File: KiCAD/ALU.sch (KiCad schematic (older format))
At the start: 55 parts, among them Q501 Q_NPN_CBE, Q502 Q_NPN_CBE, U501 74LS86AN, U502 74HCT32N, U503 74HCT32N, U504 74LS04, U505 74HCT157N, U506 74LS86AN, U507 74LS153, U508 74LS283N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

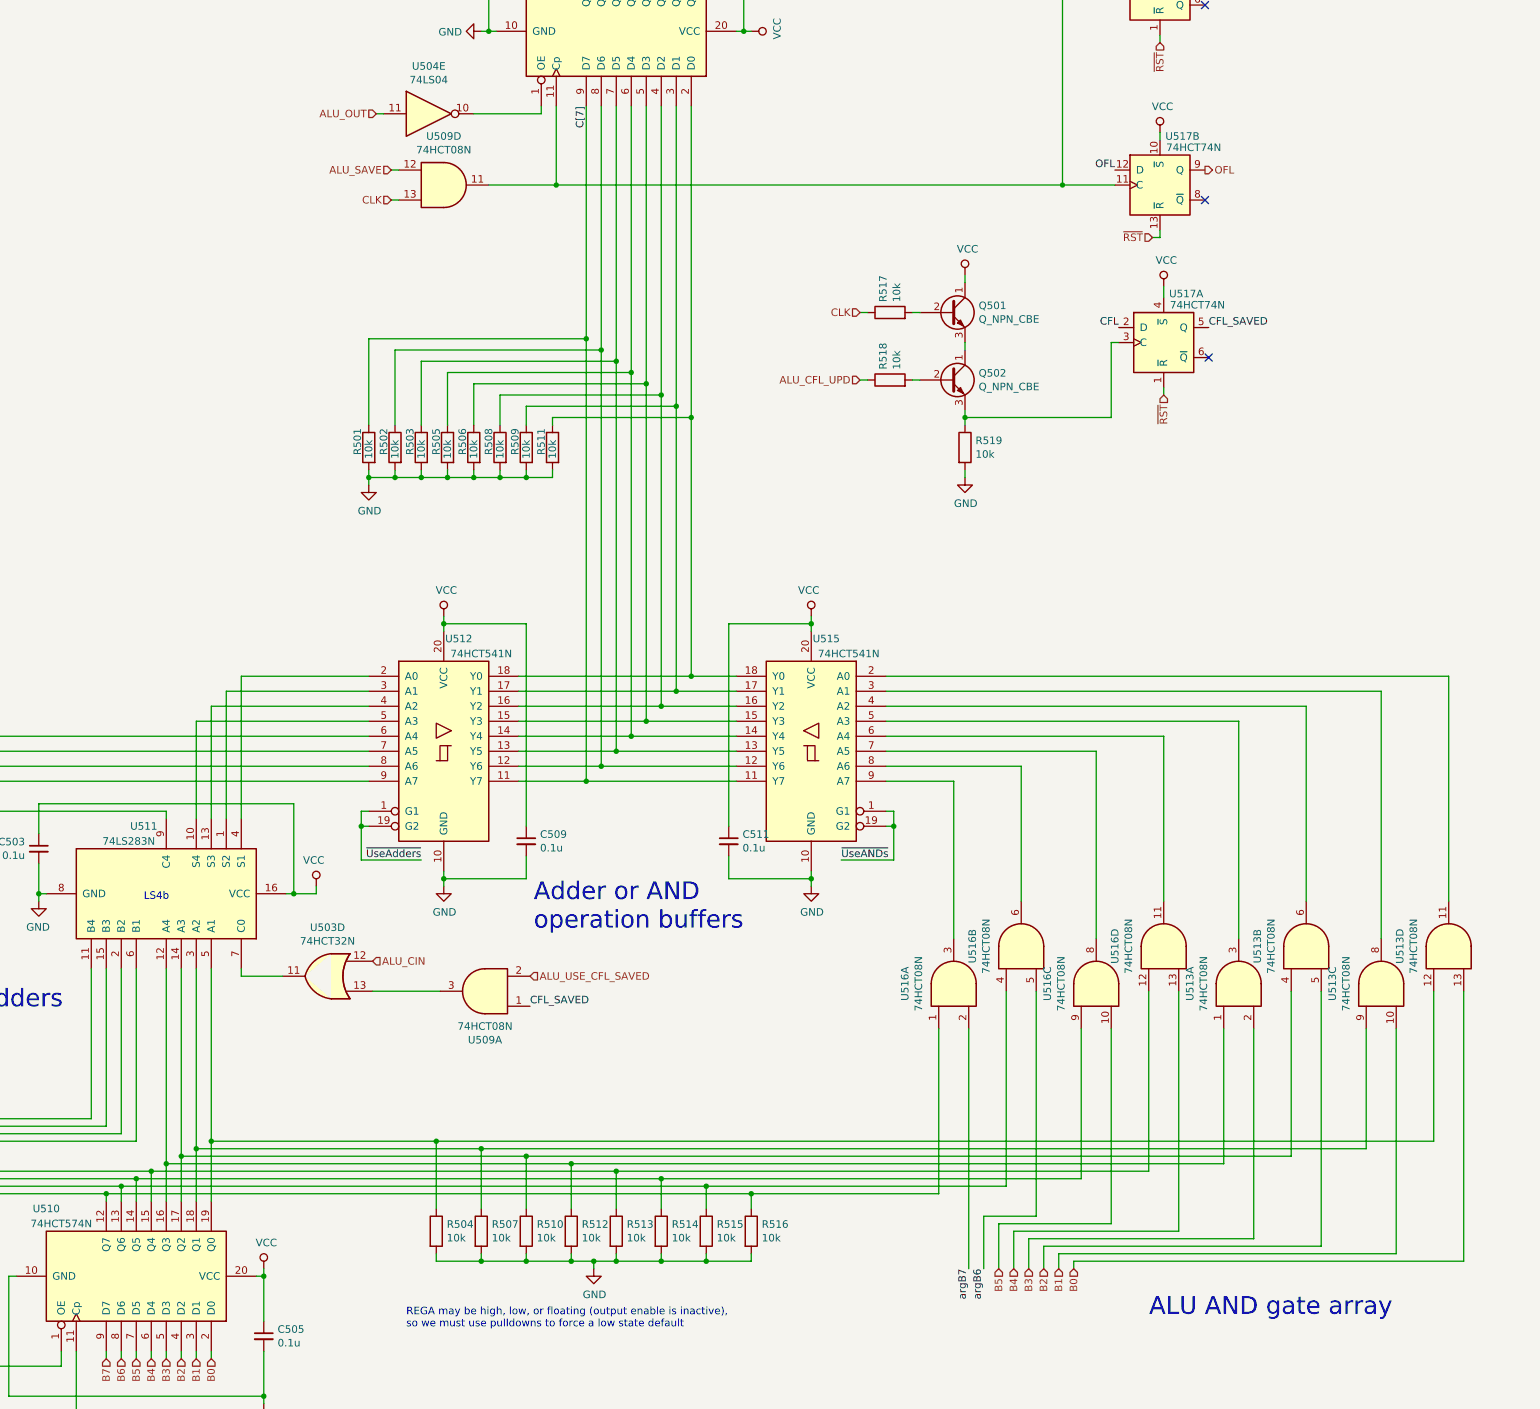
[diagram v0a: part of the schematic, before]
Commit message: Pulled ALU lines high by default.  TODO: update SP pulse circuit to reflect new TI chip design.
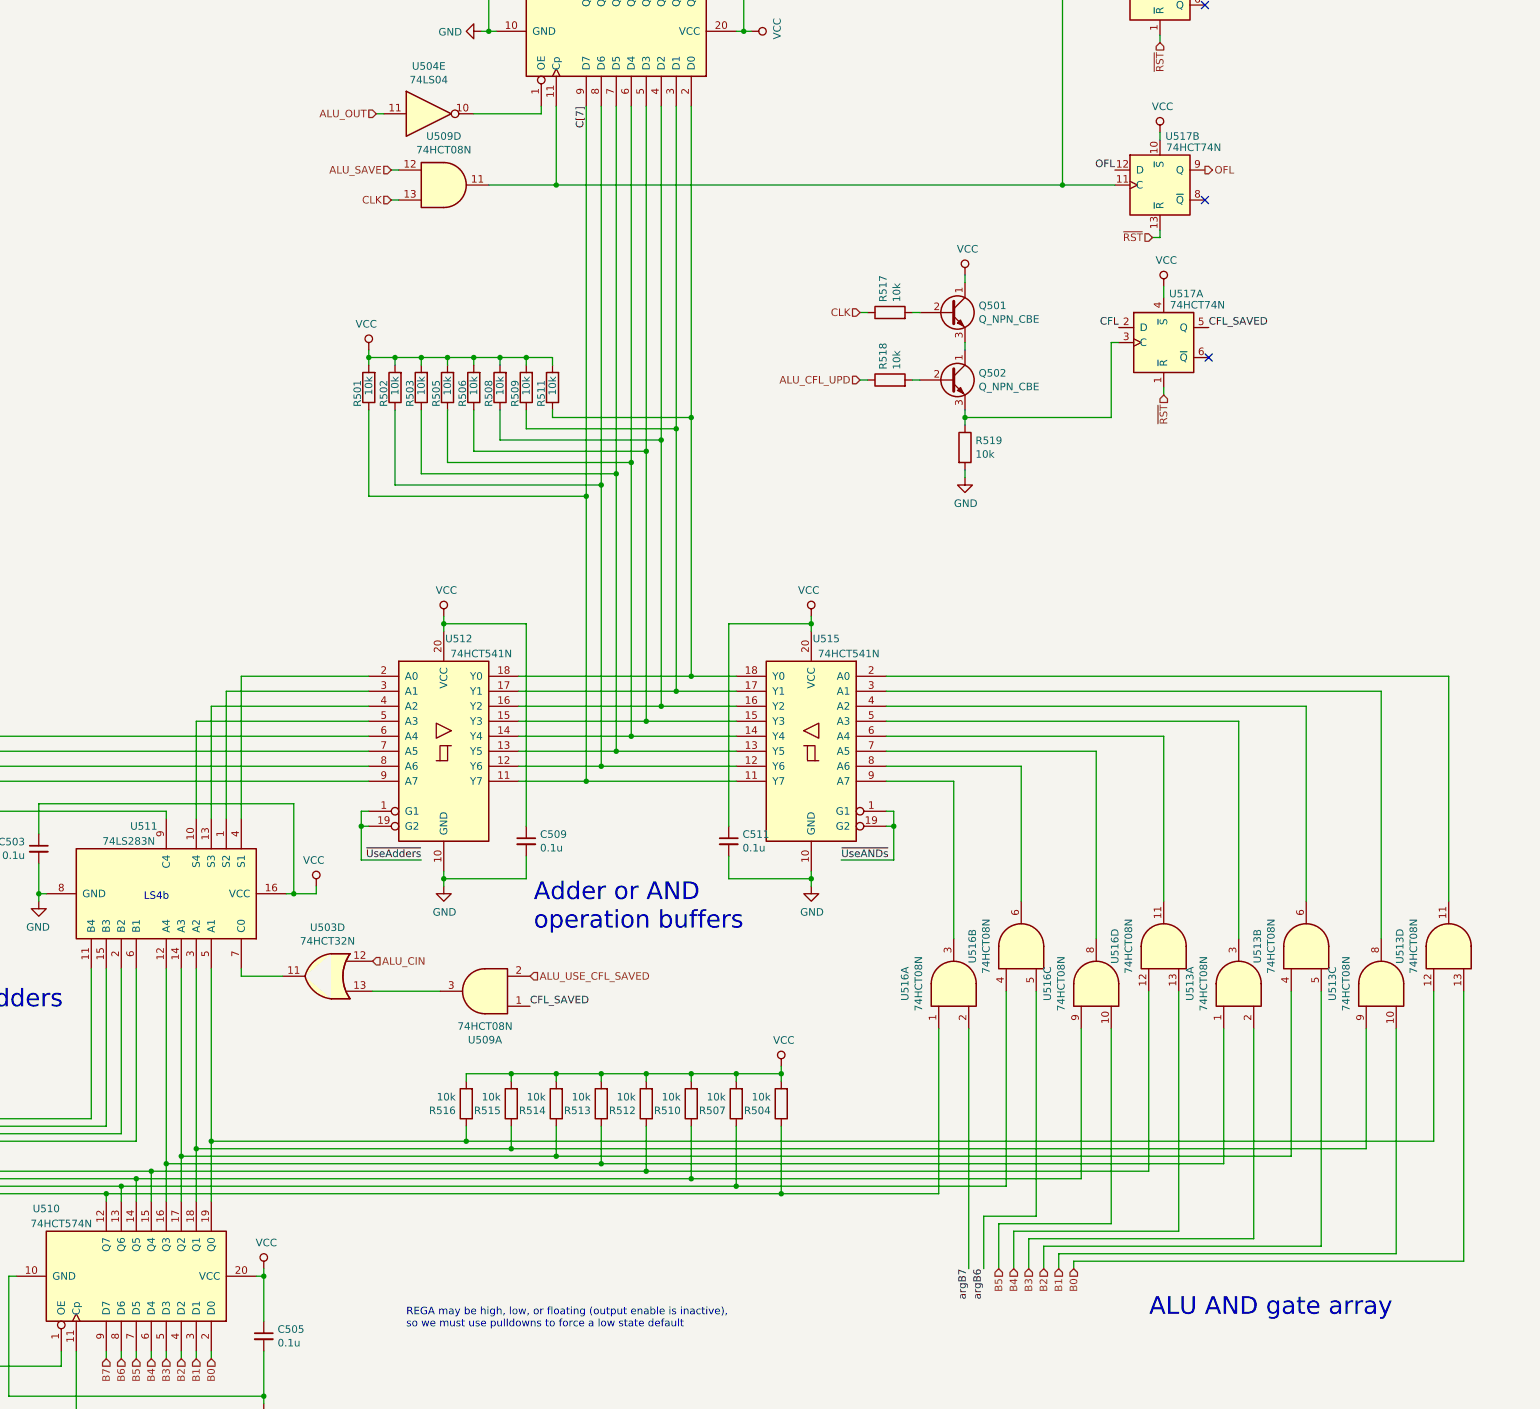
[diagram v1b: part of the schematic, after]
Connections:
- wire segments 522 -> 521
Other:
- moved on the sheet: R501, R502, R503, R504, R505, R506, R507, R508, R509, R510, R511, R512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

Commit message: Continued developing assembler
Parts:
- U507: symbol 74xx:74LS153 -> Breadboard_CPU-rescue:74LS153-74xx
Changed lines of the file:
@@
 $EndComp
 $Comp
-L 74xx:74LS153 U507
+L Breadboard_CPU-rescue:74LS153-74xx U507
 U 1 1 63DF5BEC
 P 11100 6575
